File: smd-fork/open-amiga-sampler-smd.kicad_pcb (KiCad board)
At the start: 2 copper layers, 36 x 22 mm, 18 parts, among them J1 Left, J2 Right, J3 DB25_Male, U1 ADC0820CCN, U2 MCP6001U

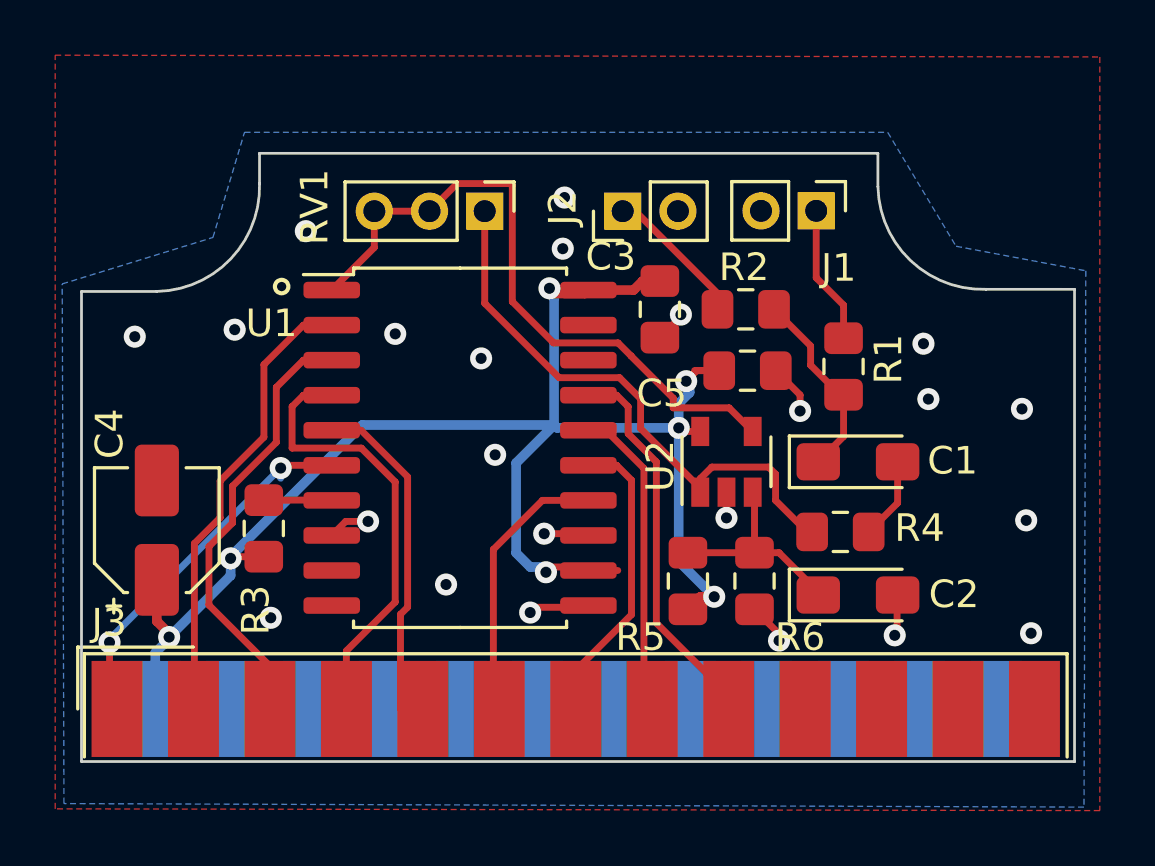
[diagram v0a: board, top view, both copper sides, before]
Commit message: re-did board outline to (maybe) actually fit
Using an accutare 3D model for a shell the board has been re-jigged to fit. still not tested against a real one though
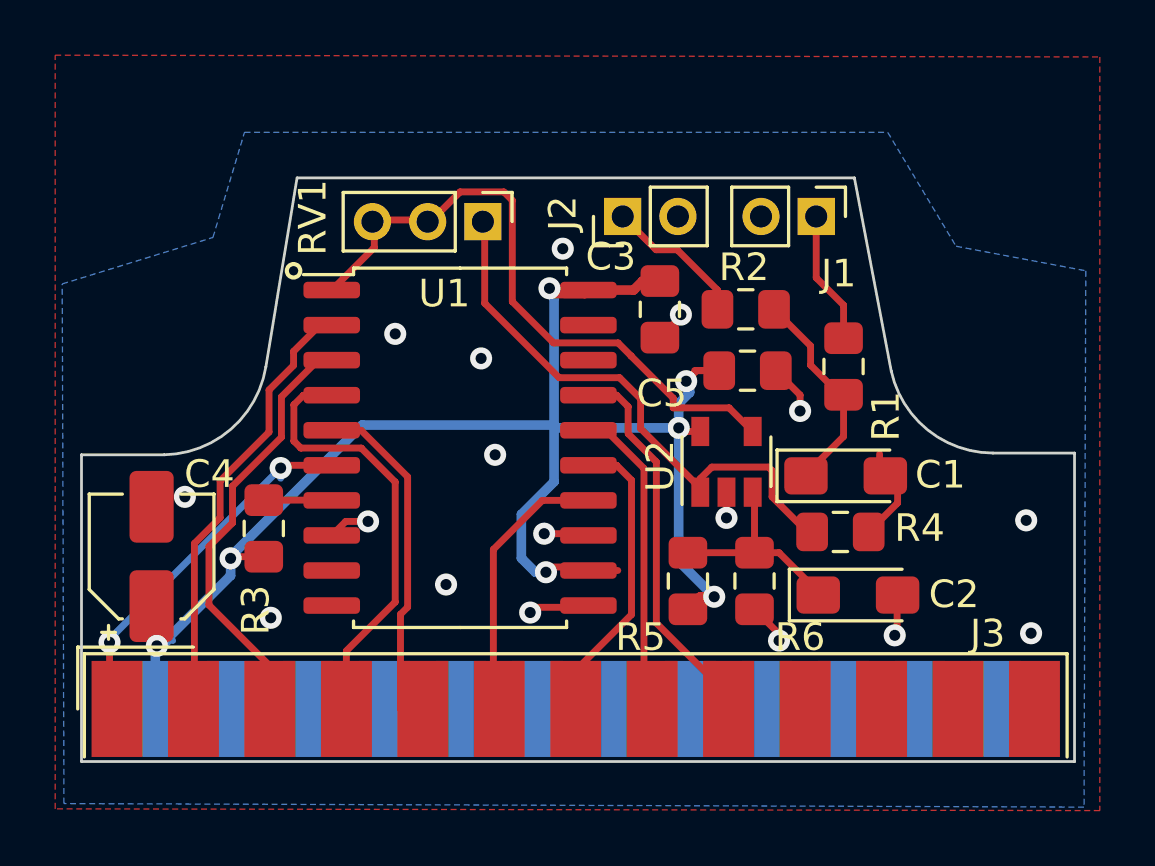
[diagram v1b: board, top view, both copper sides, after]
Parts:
- moved REF** 9.32 mm to (94.1, 140.3)
- moved C4 0.97 mm to (82.9, 143.5)
- moved C1 0.68 mm to (108.1, 140.6)
- moved RV1 0.39 mm to (94.9, 131.4)
- moved J1 0.20 mm to (107.0, 131.2)
- moved J2 0.19 mm to (100.0, 131.2)
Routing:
- net Net-(J2-Pad1): track 5.25 -> 6.27 mm
- net VCC: track 61.5 -> 60.6 mm
- net Vo: track 24.0 -> 23.3 mm
- net GND: vias 23 -> 17
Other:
- board size 36 x 22 mm -> 36 x 21.1 mm
